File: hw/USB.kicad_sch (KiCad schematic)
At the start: 3 parts, among them J2 USB_C_Receptacle_USB2.0

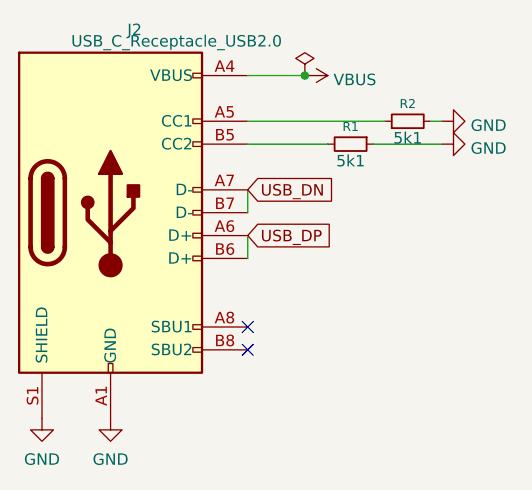
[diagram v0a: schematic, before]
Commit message: hw: multiplex Game Boy bus pins
Signed-off-by: Mahyar Koshkouei <mk@deltabeard.com>
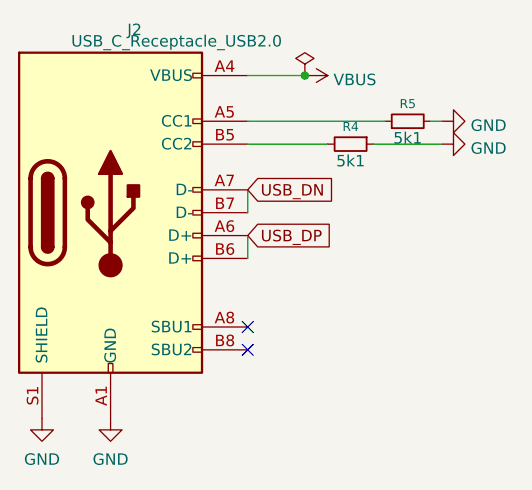
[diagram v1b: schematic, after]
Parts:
- renumbered R1 to R4, R2 to R5
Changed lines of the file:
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@@
   (symbol (lib_id "power:VBUS") (at 95.25 72.39 270) (unit 1)
     (in_bom yes) (on_board yes) (fields_autoplaced)
-    (property "Reference" "#PWR024" (id 0) (at 91.44 72.39 0)
+    (property "Reference" "#PWR026" (id 0) (at 91.44 72.39 0)
       (effects (font (size 1.27 1.27)) hide)
     )
@@
   (symbol (lib_id "power:GND") (at 66.04 110.49 0) (unit 1)
     (in_bom yes) (on_board yes) (fields_autoplaced)
-    (property "Reference" "#PWR022" (id 0) (at 66.04 116.84 0)
+    (property "Reference" "#PWR024" (id 0) (at 66.04 116.84 0)
       (effects (font (size 1.27 1.27)) hide)
     )
@@
   (symbol (lib_id "power:GND") (at 73.66 110.49 0) (unit 1)
     (in_bom yes) (on_board yes) (fields_autoplaced)
-    (property "Reference" "#PWR023" (id 0) (at 73.66 116.84 0)
+    (property "Reference" "#PWR025" (id 0) (at 73.66 116.84 0)
       (effects (font (size 1.27 1.27)) hide)
     )
@@
   (symbol (lib_id "power:GND") (at 110.49 77.47 90) (unit 1)
     (in_bom yes) (on_board yes) (fields_autoplaced)
-    (property "Reference" "#PWR025" (id 0) (at 116.84 77.47 0)
+    (property "Reference" "#PWR027" (id 0) (at 116.84 77.47 0)
       (effects (font (size 1.27 1.27)) hide)
     )
@@
   (symbol (lib_id "power:GND") (at 110.49 80.01 90) (unit 1)
     (in_bom yes) (on_board yes) (fields_autoplaced)
-    (property "Reference" "#PWR026" (id 0) (at 116.84 80.01 0)
+    (property "Reference" "#PWR028" (id 0) (at 116.84 80.01 0)
       (effects (font (size 1.27 1.27)) hide)
     )
@@
   (symbol (lib_id "Device:R_Small") (at 100.33 80.01 270) (unit 1)
     (in_bom yes) (on_board yes)
-    (property "Reference" "R1" (id 0) (at 100.33 78.0818 90)
+    (property "Reference" "R4" (id 0) (at 100.33 78.0818 90)
       (effects (font (size 1 1)))
     )
@@
   (symbol (lib_id "Device:R_Small") (at 106.68 77.47 90) (unit 1)
     (in_bom yes) (on_board yes)
-    (property "Reference" "R2" (id 0) (at 106.68 75.5418 90)
+    (property "Reference" "R5" (id 0) (at 106.68 75.5418 90)
       (effects (font (size 1 1)))
     )

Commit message: hw: WIP
Signed-off-by: Mahyar Koshkouei <mk@deltabeard.com>
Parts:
- R4, R5: footprint Resistor_SMD:R_0603_1608Metric -> Resistor_SMD:R_0402_1005Metric; LCSC C23186 -> C25905; MFr 0603WAF5101T5E -> 0402WGF5101TCE; Manufacturer UNI-ROYAL(Uniroyal Elec) -> UNI-ROYAL(Uniroyal Elec)
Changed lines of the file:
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@@
     )
     (property "Value" "5k1" (id 1) (at 100.33 81.8919 90))
-    (property "Footprint" "Resistor_SMD:R_0603_1608Metric" (id 2) (at 100.33 80.01 0)
+    (property "Footprint" "Resistor_SMD:R_0402_1005Metric" (id 2) (at 100.33 80.01 0)
       (effects (font (size 1.27 1.27)) hide)
     )
@@
       (effects (font (size 1.27 1.27)) hide)
     )
-    (property "LCSC" "C23186" (id 4) (at 100.33 80.01 0)
+    (property "LCSC" "C25905" (id 4) (at 100.33 80.01 0)
       (effects (font (size 1.27 1.27)) hide)
     )
-    (property "Description" "±1% ±100ppm/℃ 5.1kΩ 0.1W 0603 Chip Resistor - Surface Mount ROHS " (id 5) (at 100.33 80.01 0)
+    (property "Description" "±1% 1/16W ±100ppm/℃ 5.1kΩ 0402 Chip Resistor - Surface Mount ROHS" (id 5) (at 100.33 80.01 0)
       (effects (font (size 1.27 1.27)) hide)
     )
-    (property "MFr" "0603WAF5101T5E" (id 6) (at 100.33 80.01 0)
+    (property "MFr" "0402WGF5101TCE" (id 6) (at 100.33 80.01 0)
       (effects (font (size 1.27 1.27)) hide)
     )
-    (property "Manufacturer" " UNI-ROYAL(Uniroyal Elec) " (id 7) (at 100.33 80.01 0)
+    (property "Manufacturer" "UNI-ROYAL(Uniroyal Elec) " (id 7) (at 100.33 80.01 0)
       (effects (font (size 1.27 1.27)) hide)
     )
@@
     )
     (property "Value" "5k1" (id 1) (at 106.68 79.3519 90))
-    (property "Footprint" "Resistor_SMD:R_0603_1608Metric" (id 2) (at 106.68 77.47 0)
+    (property "Footprint" "Resistor_SMD:R_0402_1005Metric" (id 2) (at 106.68 77.47 0)
       (effects (font (size 1.27 1.27)) hide)
     )
@@
       (effects (font (size 1.27 1.27)) hide)
     )
-    (property "LCSC" "C23186" (id 4) (at 106.68 77.47 0)
+    (property "LCSC" "C25905" (id 4) (at 106.68 77.47 0)
       (effects (font (size 1.27 1.27)) hide)
     )
-    (property "Description" "±1% ±100ppm/℃ 5.1kΩ 0.1W 0603 Chip Resistor - Surface Mount ROHS " (id 5) (at 106.68 77.47 0)
+    (property "Description" "±1% 1/16W ±100ppm/℃ 5.1kΩ 0402 Chip Resistor - Surface Mount ROHS" (id 5) (at 106.68 77.47 0)
       (effects (font (size 1.27 1.27)) hide)
     )
-    (property "MFr" "0603WAF5101T5E" (id 6) (at 106.68 77.47 0)
+    (property "MFr" "0402WGF5101TCE" (id 6) (at 106.68 77.47 0)
       (effects (font (size 1.27 1.27)) hide)
     )
-    (property "Manufacturer" " UNI-ROYAL(Uniroyal Elec) " (id 7) (at 106.68 77.47 0)
+    (property "Manufacturer" "UNI-ROYAL(Uniroyal Elec) " (id 7) (at 106.68 77.47 0)
       (effects (font (size 1.27 1.27)) hide)
     )
